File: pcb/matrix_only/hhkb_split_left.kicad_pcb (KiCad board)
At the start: 2 copper layers, 140.4 x 97.4 mm, 65 parts, among them SW1 CPG151101S11-2, SW10 CPG151101S11-2, SW11 CPG151101S11-2, SW12 CPG151101S11-2, SW13 CPG151101S11-2, SW14 CPG151101S11-2, SW15 CPG151101S11-2, SW16 CPG151101S11-2, SW17 CPG151101S11-2, SW18 CPG151101S11-2, SW19 CPG151101S11-2, SW2 CPG151101S11-2, SW20 CPG151101S11-2, SW21 CPG151101S11-2, SW22 CPG151101S11-2, SW23 CPG151101S11-2, SW24 CPG151101S11-2, SW25 CPG151101S11-2, SW26 CPG151101S11-2, SW27 CPG151101S11-2, SW3 CPG151101S11-2, SW4 CPG151101S11-2, SW5 CPG151101S11-2, SW6 CPG151101S11-2, SW7 CPG151101S11-2, SW8 CPG151101S11-2, SW9 CPG151101S11-2, U1 74LVC595

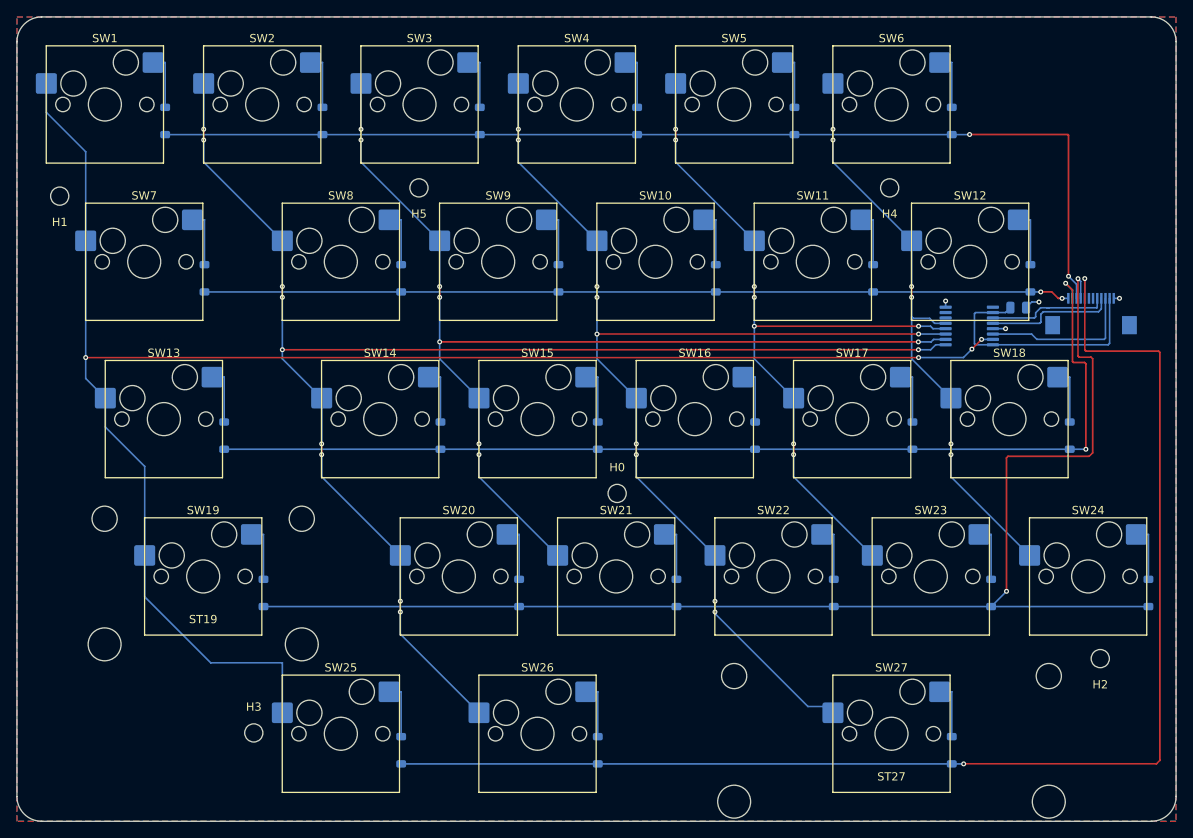
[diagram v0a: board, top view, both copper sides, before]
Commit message: #51 の基板一式——3 枚とも DRC 違反 0 / 未配線 0
利用者が右の J_DB 周り 9 ネットを新しい位置へ引き直し（matrix_only）、
V3V3 の切れ目と、写しの φ0.5→0.56 化で近すぎたビア 3 ペアも修正。
写し（matrix_routing.json）→ gen_pcb（外形 左 138.4 / 右 171.7）→
finalize --src unrouted → DRC の全経路を通した。部品位置の写しを含む。

Co-Authored-By: Claude Fable 5 <noreply@anthropic.com>
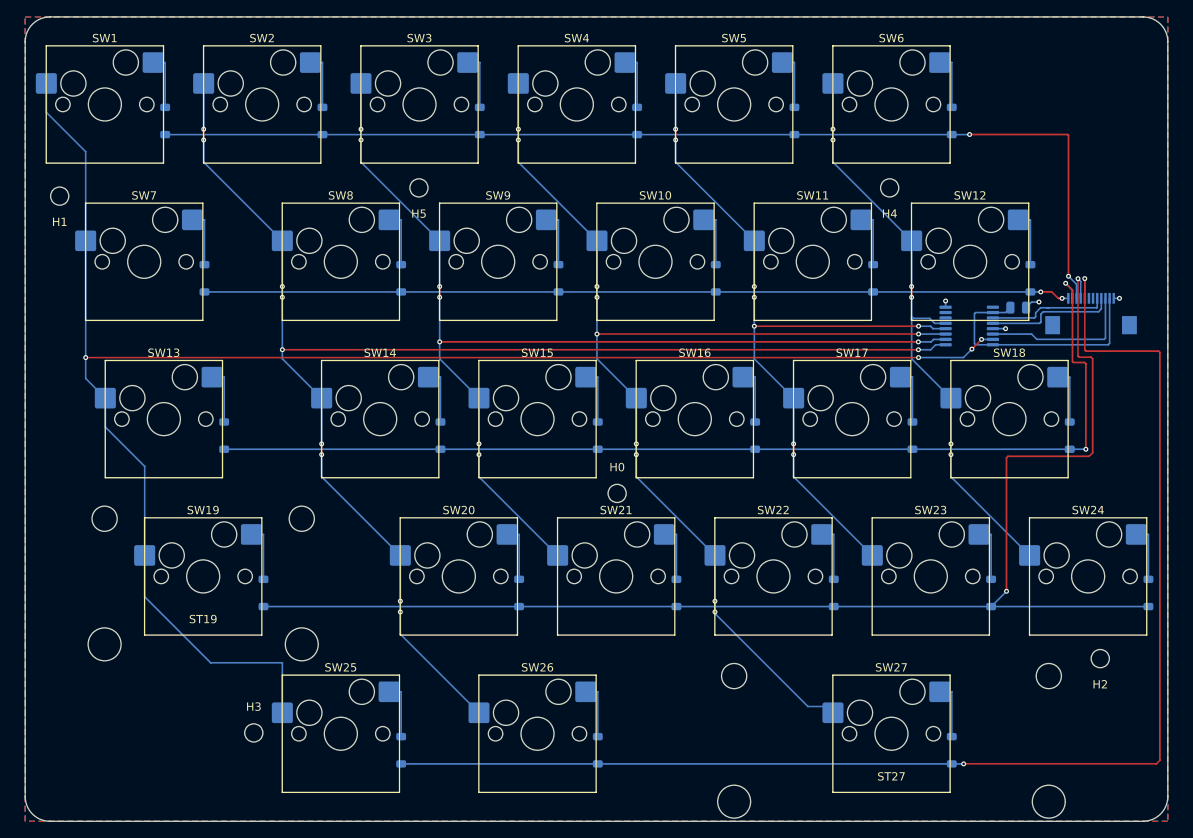
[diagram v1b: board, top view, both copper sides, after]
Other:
- board size 140.4 x 97.4 mm -> 138.4 x 97.4 mm

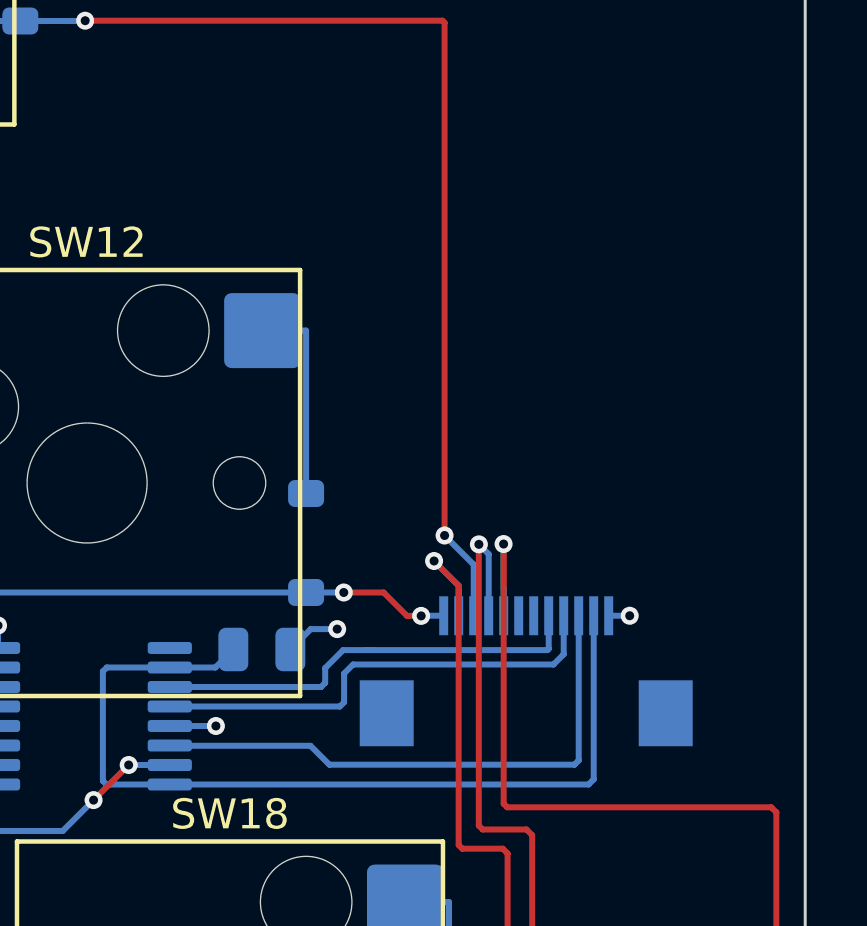
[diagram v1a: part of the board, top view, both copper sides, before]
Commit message: #49 オシロ用テストパッドを実装した（左 5・右 6・実装なしのランド）
利用者の決定（Yes）。信号は SPI_SCK / SPI_MOSI / CS / V3V3 / GND、右は
595 の数珠つなぎ U1_U2 も。ROW/COL はダイオードとソケットのパッドで
見られるので出さない。kind `testpoint` を回路宣言・pinmap・
parts.NOT_ASSEMBLED（BOM/CPL に出さない）・回路図の群・gen_pcb の
絶対座標配置（TP_PLACE・本番の板の空きを実測して決めた）に通した。

検査側の修正: TestPoint 系フットプリントの円コートヤードを
_courtyard_bbox が読めず「コートヤード無し」と誤判定していた（四角を
足したら自己交差になって発覚）→ fp_circle も読む。

残り: 各パッドから既存ネットへのスタブ（GND 以外）を利用者が引く
（左 4・右 5）。引くまで DRC の未配線がその本数ぶん残る。

Co-Authored-By: Claude Fable 5 <noreply@anthropic.com>
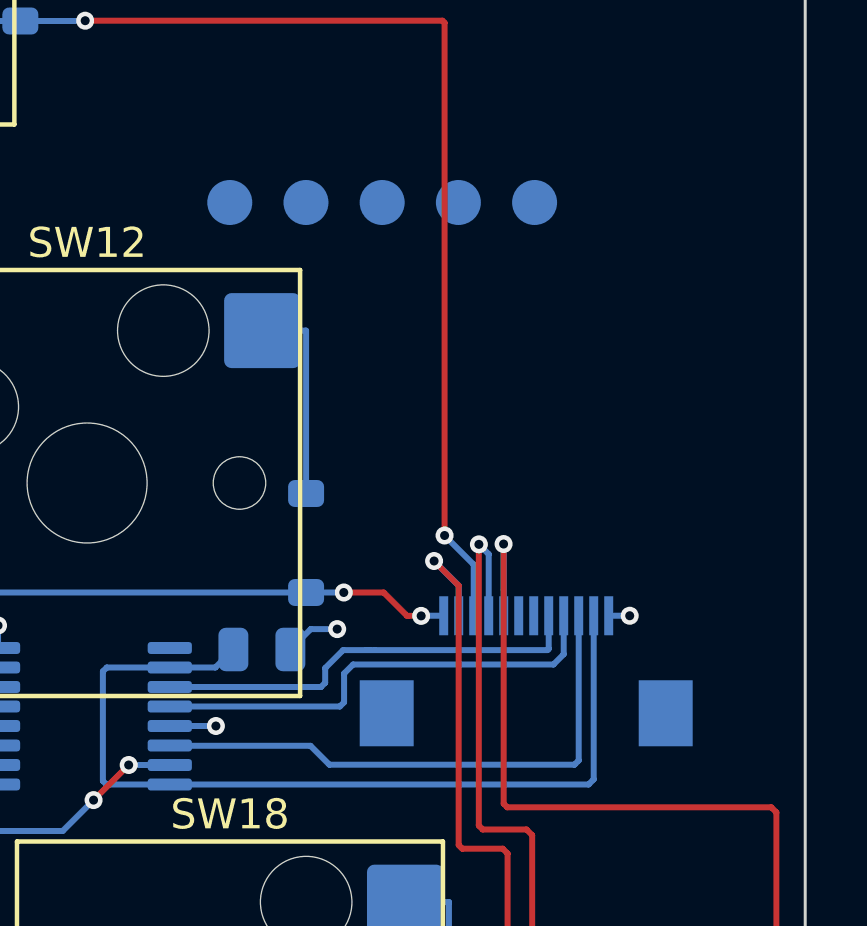
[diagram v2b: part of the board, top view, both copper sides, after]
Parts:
- added TP1: testpoint, TestPoint_Pad_D1.5mm, B.Cu at (200.0, 71.6)
- added TP2: testpoint, TestPoint_Pad_D1.5mm, B.Cu at (202.5, 71.6)
- added TP3: testpoint, TestPoint_Pad_D1.5mm, B.Cu at (205.1, 71.6)
- added TP4: testpoint, TestPoint_Pad_D1.5mm, B.Cu at (207.6, 71.6)
- added TP5: testpoint, TestPoint_Pad_D1.5mm, B.Cu at (210.2, 71.6)

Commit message: Revert "#49 オシロ用テストパッドを実装した"——利用者が取り消しを決定
パッドから既存ネットへのスタブが引けず（利用者「試行錯誤したが諦める」）。
代案（利用者提案）: 既存のビアのレジストを剥がしてリード線を半田付けできる
ようにする。部品追加も配線も不要。別コミットで実装する。
検査側の修正（_courtyard_bbox が fp_circle も読む）だけは有用なので残す。

This reverts commits b8ea548 and 4f7bba2 (except the test improvement).

Co-Authored-By: Claude Fable 5 <noreply@anthropic.com>
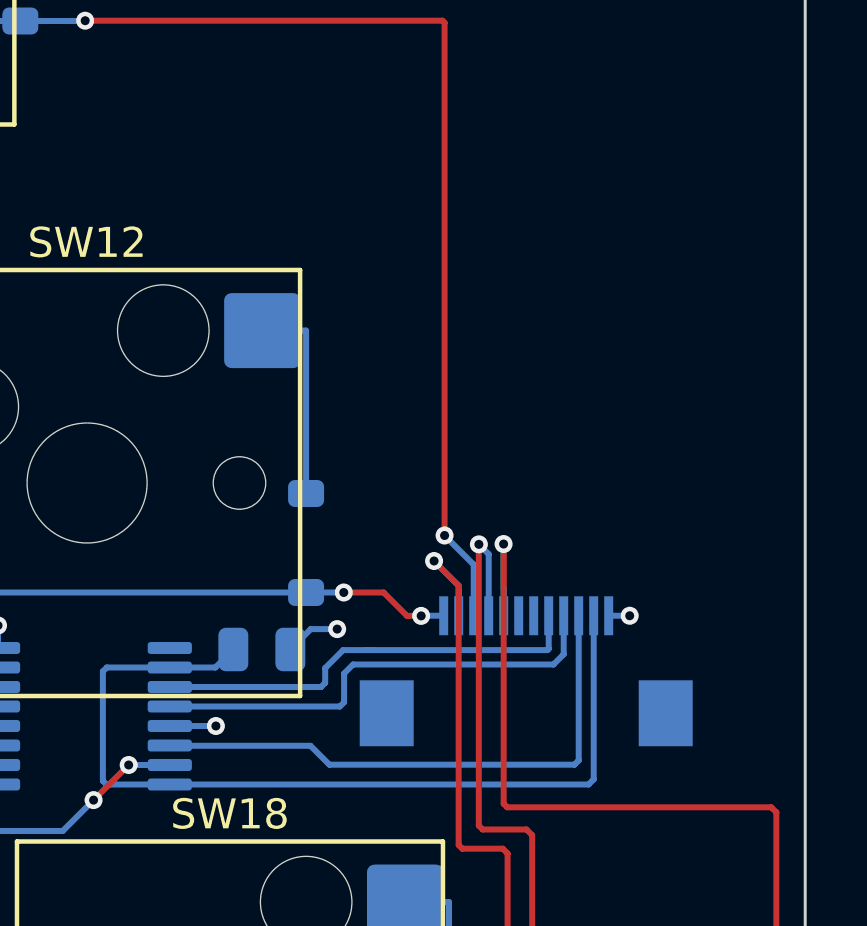
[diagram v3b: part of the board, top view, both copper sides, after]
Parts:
- removed TP1, TP2, TP3, TP4, TP5: testpoint, TestPoint_Pad_D1.5mm

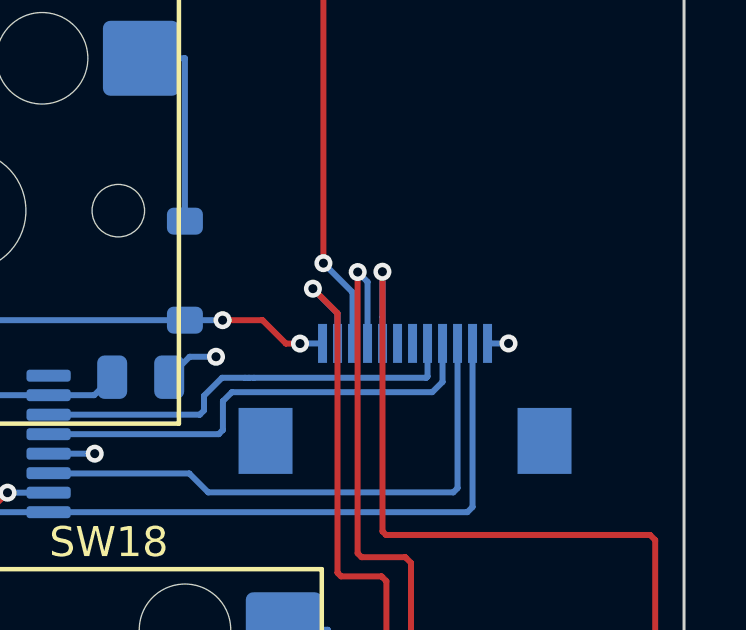
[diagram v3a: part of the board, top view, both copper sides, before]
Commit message: #49 露出規則の「部品本体」を Fab 外形に統一し、利用者の左ビア 2 個を取り込んだ——全ネット露出・検査緑
- ソケットに bands.SOCK_*（ケース側の帯）、電子部品にコートヤードを使っていて
  届くビア（右 U1_U2・左 SPI_SCK/V3V3）を弾いていた。実物の外形（Fab 図形）へ
- 左右とも 5 ネット + GND を露出。DRC 3 枚 違反 0（左 +2 は利用者ビアの via_dangling）
- 部品記録・DRC 記録・open-gaps #49・記録資料 項目 25 を更新

Co-Authored-By: Claude Fable 5 <noreply@anthropic.com>
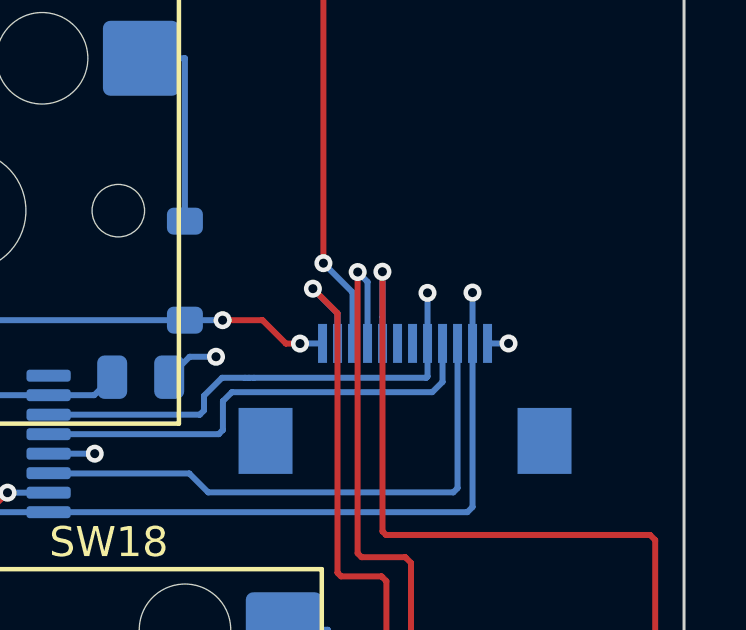
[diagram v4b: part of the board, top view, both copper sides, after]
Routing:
- net V3V3: track 30.2 -> 31.9 mm, vias 0 -> 1
- net SPI_SCK: track 14.5 -> 16.2 mm, vias 0 -> 1

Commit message: #49 左 SPI_MOSI / CS にも利用者のビア——左右 5+5 ネットを全部ビアで露出（配線の窓なし）
- DRC 3 枚 違反 0（左 +2 は新ビアの via_dangling）・test_pcb 79 緑
- 部品記録・DRC 記録・open-gaps #49・記録資料 項目 25 を更新

Co-Authored-By: Claude Fable 5 <noreply@anthropic.com>
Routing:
- net CS: track 15.7 -> 18.3 mm, vias 0 -> 1
- net SPI_MOSI: vias 0 -> 1
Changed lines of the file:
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@@
 		(net "V3V3")
+	)
+	(via
+		(at 202.69 89.71)
+		(size 0.6)
+		(drill 0.3)
+		(layers "F.Cu" "B.Cu")
+		(net "SPI_MOSI")
 	)
 	(segment
@@
 		(net "SPI_MOSI")
 	)
+	(via
+		(at 211.32 82.88)
+		(size 0.6)
+		(drill 0.3)
+		(layers "F.Cu" "B.Cu")
+		(net "CS")
+	)
 	(segment
 		(start 210.79 87)
@@
 	)
 	(segment
+		(start 211.13125 84.25875)
+		(end 211.32 84.07)
+		(width 0.2)
+		(layer "B.Cu")
+		(net "CS")
+	)
+	(segment
+		(start 211.13125 85.375)
+		(end 211.13125 84.25875)
+		(width 0.2)
+		(layer "B.Cu")
+		(net "CS")
+	)
+	(segment
 		(start 203.67 88.4)
 		(end 203.81 88.26)
 		(width 0.2)
 		(layer "B.Cu")
+		(net "CS")
+	)
+	(segment
+		(start 211.32 84.07)
+		(end 211.32 82.88)
+		(width 0.2)
+		(layer "B.Cu")

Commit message: #49 SPARE/SPARE2（XIAO D4/D9）を主基板で露出——I2C などの拡張用。右の J_DB 周りのビアを φ0.6 に統一
- 利用者が matrix_only で J_DB パッド 6・7 から枝＋ビアを手で打った（左右）
- pcb_rules.DEBUG_NETS に 2 ネットを追加、finalize_pcb で本番へ
- 右の φ0.5/0.3 ビア 17 個（アニュラー 0.10 < 0.13）を φ0.6 に揃え、違反 17 → 0
- DRC 3 枚 違反 0 / 未配線 0。検査 151 緑。export_fab リハーサル通過（B.Mask 開口 4 点確認）
- 記録: open-gaps #49・fab-checklist 4b・pcb_parts / product_groups

Co-Authored-By: Claude Fable 5 <noreply@anthropic.com>
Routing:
- net SPARE2: track 0.00 -> 4.48 mm, vias 0 -> 1
- net SPARE: track 0.00 -> 4.03 mm, vias 0 -> 1
- net SPI_SCK: track 16.2 -> 18.4 mm
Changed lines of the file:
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@@
 	)
 	(via
-		(at 211.32 82.88)
+		(at 211.53 82.76)
 		(size 0.6)
 		(drill 0.3)
@@
 	)
 	(segment
+		(start 211.13125 84.530221)
+		(end 211.53 84.131471)
+		(width 0.2)
+		(layer "B.Cu")
+		(net "CS")
+	)
+	(segment
 		(start 204.11 87)
 		(end 210.79 87)
@@
 	)
 	(segment
-		(start 211.13125 84.25875)
-		(end 211.32 84.07)
-		(width 0.2)
-		(layer "B.Cu")
-		(net "CS")
-	)
-	(segment
-		(start 211.13125 85.375)
-		(end 211.13125 84.25875)
+		(start 211.53 82.76)
+		(end 211.68 82.76)
+		(width 0.2)
+		(layer "B.Cu")
+		(net "CS")
+	)
+	(segment
+		(start 211.53 84.131471)
+		(end 211.53 82.76)
 		(width 0.2)
 		(layer "B.Cu")
@@
 	)
 	(segment
-		(start 211.32 84.07)
-		(end 211.32 82.88)
-		(width 0.2)
-		(layer "B.Cu")
-		(net "CS")
-	)
-	(segment
 		(start 211.1312 86.6587)
 		(end 211.1312 85.375)
@@
 		(net "CS")
 	)
-	(via
-		(at 210.63 83.69)
-		(size 0.6)
-		(drill 0.3)
-		(layers "F.Cu" "B.Cu")
+	(segment
+		(start 211.13125 85.375)
+		(end 211.13125 84.530221)
+		(width 0.2)
+		(layer "B.Cu")
+		(net "CS")
+	)
+	(via
+		(at 211.24 81.77)
+		(size 0.6)
+		(drill 0.3)
+		(layers "F.Cu" "B.Cu")
+		(net "SPI_SCK")
+	)
+	(segment
+		(start 210.63125 85.375)
+		(end 210.63125 84.39875)
+		(width 0.2)
+		(layer "B.Cu")
 		(net "SPI_SCK")
 	)
@@
 	)
 	(segment
+		(start 210.63125 84.39875)
+		(end 210.93 84.1)
+		(width 0.2)
+		(layer "B.Cu")
+		(net "SPI_SCK")
+	)
+	(segment
 		(start 204.54 86.52)
 		(end 203.78 86.52)
@@
 	)
 	(segment
-		(start 210.63125 85.375)
-		(end 210.63125 83.69125)
+		(start 210.93 84.1)
+		(end 210.93 82.08)
 		(width 0.2)
 		(layer "B.Cu")
@@
 	)
 	(segment
+		(start 210.93 82.08)
+		(end 211.24 81.77)
+		(width 0.2)
+		(layer "B.Cu")
+		(net "SPI_SCK")
+	)
+	(segment
 		(start 203.18 87.61)
 		(end 203.04 87.75)
@@
 		(net "SPI_SCK")
 	)
+	(via
+		(at 210.53 81.06)
+		(size 0.6)
+		(drill 0.3)
+		(layers "F.Cu" "B.Cu")
+		(net "SPARE2")
+	)
+	(segment
+		(start 210.13125 84.32875)
+		(end 210.53 83.93)
+		(width 0.2)
+		(layer "B.Cu")
+		(net "SPARE2")
+	)
+	(segment
+		(start 210.53 83.93)
+		(end 210.53 81.06)
+		(width 0.2)
+		(layer "B.Cu")
+		(net "SPARE2")
+	)
+	(segment
+		(start 210.13125 85.375)
+		(end 210.13125 84.32875)
+		(width 0.2)
+		(layer "B.Cu")
+		(net "SPARE2")
+	)
+	(via
+		(at 209.71 81.59)
+		(size 0.6)
+		(drill 0.3)
+		(layers "F.Cu" "B.Cu")
+		(net "SPARE")
+	)
+	(segment
+		(start 209.63125 85.375)
+		(end 209.63125 84.263064)
+		(width 0.2)
+		(layer "B.Cu")
+		(net "SPARE")
+	)
+	(segment
+		(start 209.63125 84.263064)
+		(end 209.965565 83.92875)
+		(width 0.2)
+		(layer "B.Cu")
+		(net "SPARE")
+	)
+	(segment
+		(start 209.97 81.85)
+		(end 209.71 81.59)
+		(width 0.2)
+		(layer "B.Cu")
+		(net "SPARE")
+	)
+	(segment
+		(start 209.965565 83.92875)
+		(end 209.965565 81.854435)
+		(width 0.2)
+		(layer "B.Cu")
+		(net "SPARE")
+	)
+	(segment
+		(start 209.965565 81.854435)
+		(end 209.97 81.85)
+		(width 0.2)
+		(layer "B.Cu")
+		(net "SPARE")
+	)
 	(zone

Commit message: #19 J_DB の口を奥向きに回した（FFC は直線・A タイプで正しい）。左は配線無傷で DRC 0、右は J_DB 周りの引き直し待ち
- 原因: 2026-08-08 の初回配置で Flip() の副作用の 180° をそのまま使い、誰も口の向きを決めていなかった（git 履歴で確認）
- circuit.py: J_DB のピン表を J_MAIN の鏡像（n ↔ 13-n）に。裏面で 180° 回すとピン 1 の側が入れ替わるため。検査 2 本と決定文書を鏡像に更新
- gen_pcb.py: J_DB に向き 0° と dy（左 -3.7 / 右 -0.4）。配置は matrix_only の現物が優先
- 左 matrix_only: J_DB を 0°・3.7mm 奥へ → 12 パッドが同じ座標に戻り配線無傷。DRC 0/0
- 右 matrix_only: 3.7mm は SW10 の NPTH がコートヤードに入るため 0.4mm 止まり。パッドが南側の枝と重なり DRC 違反 20・未配線 8（利用者の引き直し・open-gaps #19 に手順）
- gen_assembly.py: 幕と床走行を消し、口の直後の潜り＋J_MAIN までの斜めのリボンに。箱モード干渉 0
- 回路図・部品記録・DRC 記録・証拠ページを更新。検査 455 緑・5 赤（全部右の引き直しと露出ビアの打ち直しに帰着・open-gaps に列挙）

Co-Authored-By: Claude Fable 5 <noreply@anthropic.com>
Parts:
- moved J_DB 3.70 mm to (209.9, 83.5), turned to 0 degrees
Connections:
- J_DB pad 1: GND -> ROW_E
- J_DB pad 10: ROW_C -> SPI_MOSI
- J_DB pad 11: ROW_D -> V3V3
- J_DB pad 12: ROW_E -> GND
- J_DB pad 2: V3V3 -> ROW_D
- J_DB pad 3: SPI_MOSI -> ROW_C
- J_DB pad 4: CS -> ROW_B
- J_DB pad 5: SPI_SCK -> ROW_A
- J_DB pad 6: SPARE2 -> SPARE
- J_DB pad 7: SPARE -> SPARE2
- J_DB pad 8: ROW_A -> SPI_SCK
- J_DB pad 9: ROW_B -> CS

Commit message: #49 利用者が左右の露出ビア（SPARE/SPARE2）を打ち直し。右の COL0 迂回と GND ビア径を当て直し、3 基板とも DRC 0
- 左右とも SPARE/SPARE2 が露出できるようになった（左 SCK は未だ）
- ⚠️ 打った場所はコネクタの奥側＝ケーブルの通り道。南側への移動を提案（open-gaps #19）

Co-Authored-By: Claude Fable 5 <noreply@anthropic.com>
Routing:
- net SPARE: track 4.03 -> 9.81 mm
- net SPARE2: track 4.48 -> 10.2 mm
